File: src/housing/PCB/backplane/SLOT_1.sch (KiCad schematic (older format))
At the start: 1 part, among them J6 10018784-10201TLF

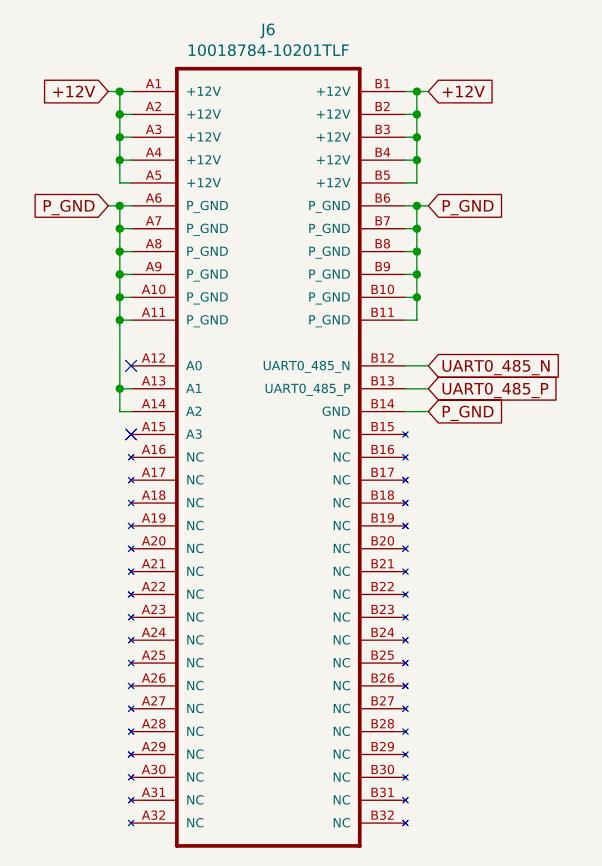
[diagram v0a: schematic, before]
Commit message: fixing backplane libraries path error
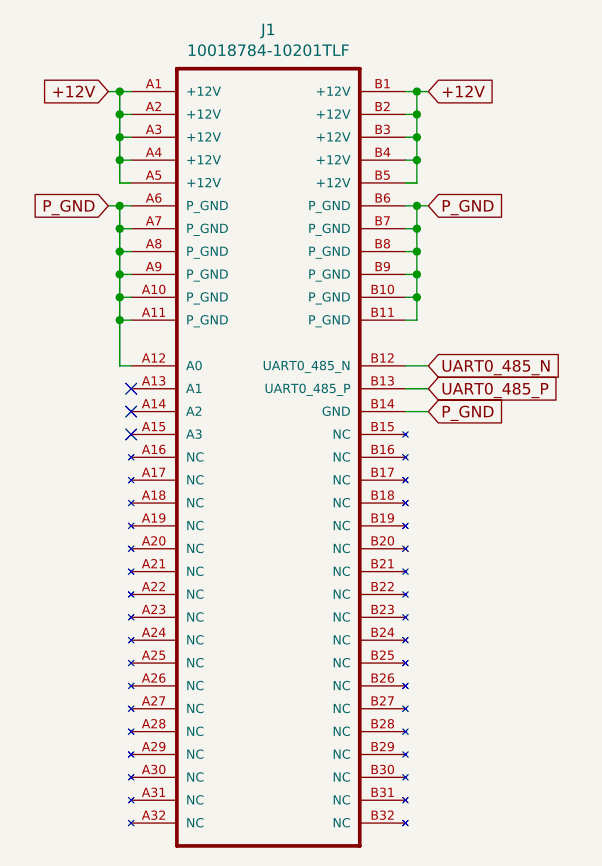
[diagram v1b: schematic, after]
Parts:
- removed J6: 10018784-10201TLF, kicad-lib:CONN_10018784-10201TLF, symbol 10018784-10201TLF:10018784-10201TLF
- added J1: 10018784-10201TLF, kicad-lib:CONN_10018784-10201TLF, symbol 10018784-10201TLF:10018784-10201TLF
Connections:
- net +12V: now also J1.A1 (+12V), J1.A2 (+12V), J1.A3 (+12V), J1.A4 (+12V), J1.A5 (+12V), J1.B1 (+12V), J1.B2 (+12V), J1.B3 (+12V), J1.B4 (+12V), J1.B5 (+12V)
- net P_GND: now also J1.A10 (P_GND), J1.A11 (P_GND), J1.A12 (A0), J1.A6 (P_GND), J1.A7 (P_GND), J1.A8 (P_GND), J1.A9 (P_GND), J1.B10 (P_GND), J1.B11 (P_GND), J1.B14 (GND), J1.B6 (P_GND), J1.B7 (P_GND), J1.B8 (P_GND), J1.B9 (P_GND)
- net UART0_485_N: now also J1.B12 (UART0_485_N)
- net UART0_485_P: now also J1.B13 (UART0_485_P)
- no-connect marks 2 -> 3
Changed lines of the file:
@@
 $Descr A4 11693 8268
 encoding utf-8
-Sheet 7 9
-Title ""
+Sheet 2 9
+Title "ACS backplane"
 Date ""
-Rev ""
-Comp ""
-Comment1 ""
+Rev "1"
+Comp "Halidelabs"
+Comment1 "contact@halidelabs.eu"
 Comment2 ""
 Comment3 ""
@@
 $EndDescr
 $Comp
-L 10018784-10201TLF:10018784-10201TLF J?
-U 1 1 5DF52F0C
+L 10018784-10201TLF:10018784-10201TLF J1
+U 1 1 5DF19CC0
 P 5600 3950
-AR Path="/5DF19C0C/5DF52F0C" Ref="J?"  Part="1"
-AR Path="/5DF2A71E/5DF52F0C" Ref="J?"  Part="1"
-AR Path="/5DF2E10A/5DF52F0C" Ref="J?"  Part="1"
-AR Path="/5DF2E1F8/5DF52F0C" Ref="J?"  Part="1"
-AR Path="/5DF2E248/5DF52F0C" Ref="J6"  Part="1"
-AR Path="/5DF2E24C/5DF52F0C" Ref="J?"  Part="1"
-F 0 "J6" H 5600 5820 50  0000 C CNN
+AR Path="/5DF19C0C/5DF19CC0" Ref="J1"  Part="1"
+AR Path="/5DF2A71E/5DF19CC0" Ref="J?"  Part="1"
+AR Path="/5DF2E10A/5DF19CC0" Ref="J?"  Part="1"
+AR Path="/5DF2E1F6/5DF19CC0" Ref="J?"  Part="1"
+AR Path="/5DF2E246/5DF19CC0" Ref="J?"  Part="1"
+AR Path="/5DF2E24A/5DF19CC0" Ref="J?"  Part="1"
+F 0 "J1" H 5600 5820 50  0000 C CNN
 F 1 "10018784-10201TLF" H 5600 5729 50  0000 C CNN
 F 2 "kicad-lib:CONN_10018784-10201TLF" H 5650 4450 50  0001 L BNN
@@
 Wire Wire Line
 	6300 3750 6200 3750
+Wire Wire Line
+	4950 3350 4950 3550
+Wire Wire Line
+	4950 3550 5000 3550
 Connection ~ 4950 3350
-Wire Wire Line
-	4950 3650 5000 3650
-Wire Wire Line
-	4950 3350 4950 3650
-Wire Wire Line
-	4950 3650 4950 3750
-Wire Wire Line
-	4950 3750 5000 3750
-Connection ~ 4950 3650
-NoConn ~ 5000 3550
+NoConn ~ 5000 3650
+NoConn ~ 5000 3750
 NoConn ~ 5000 3850
 $EndSCHEMATC
